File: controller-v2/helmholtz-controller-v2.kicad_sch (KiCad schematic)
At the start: 58 parts, among them J1 Screw_Terminal_01x02, J2 Screw_Terminal_01x02, J3 Screw_Terminal_01x02, J4 Screw_Terminal_01x02, J5 Conn_01x04, U1 BDS63150AFM, U2 BDS63150AFM, U3 INA226, U4 INA226, U5 BDS63150AFM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

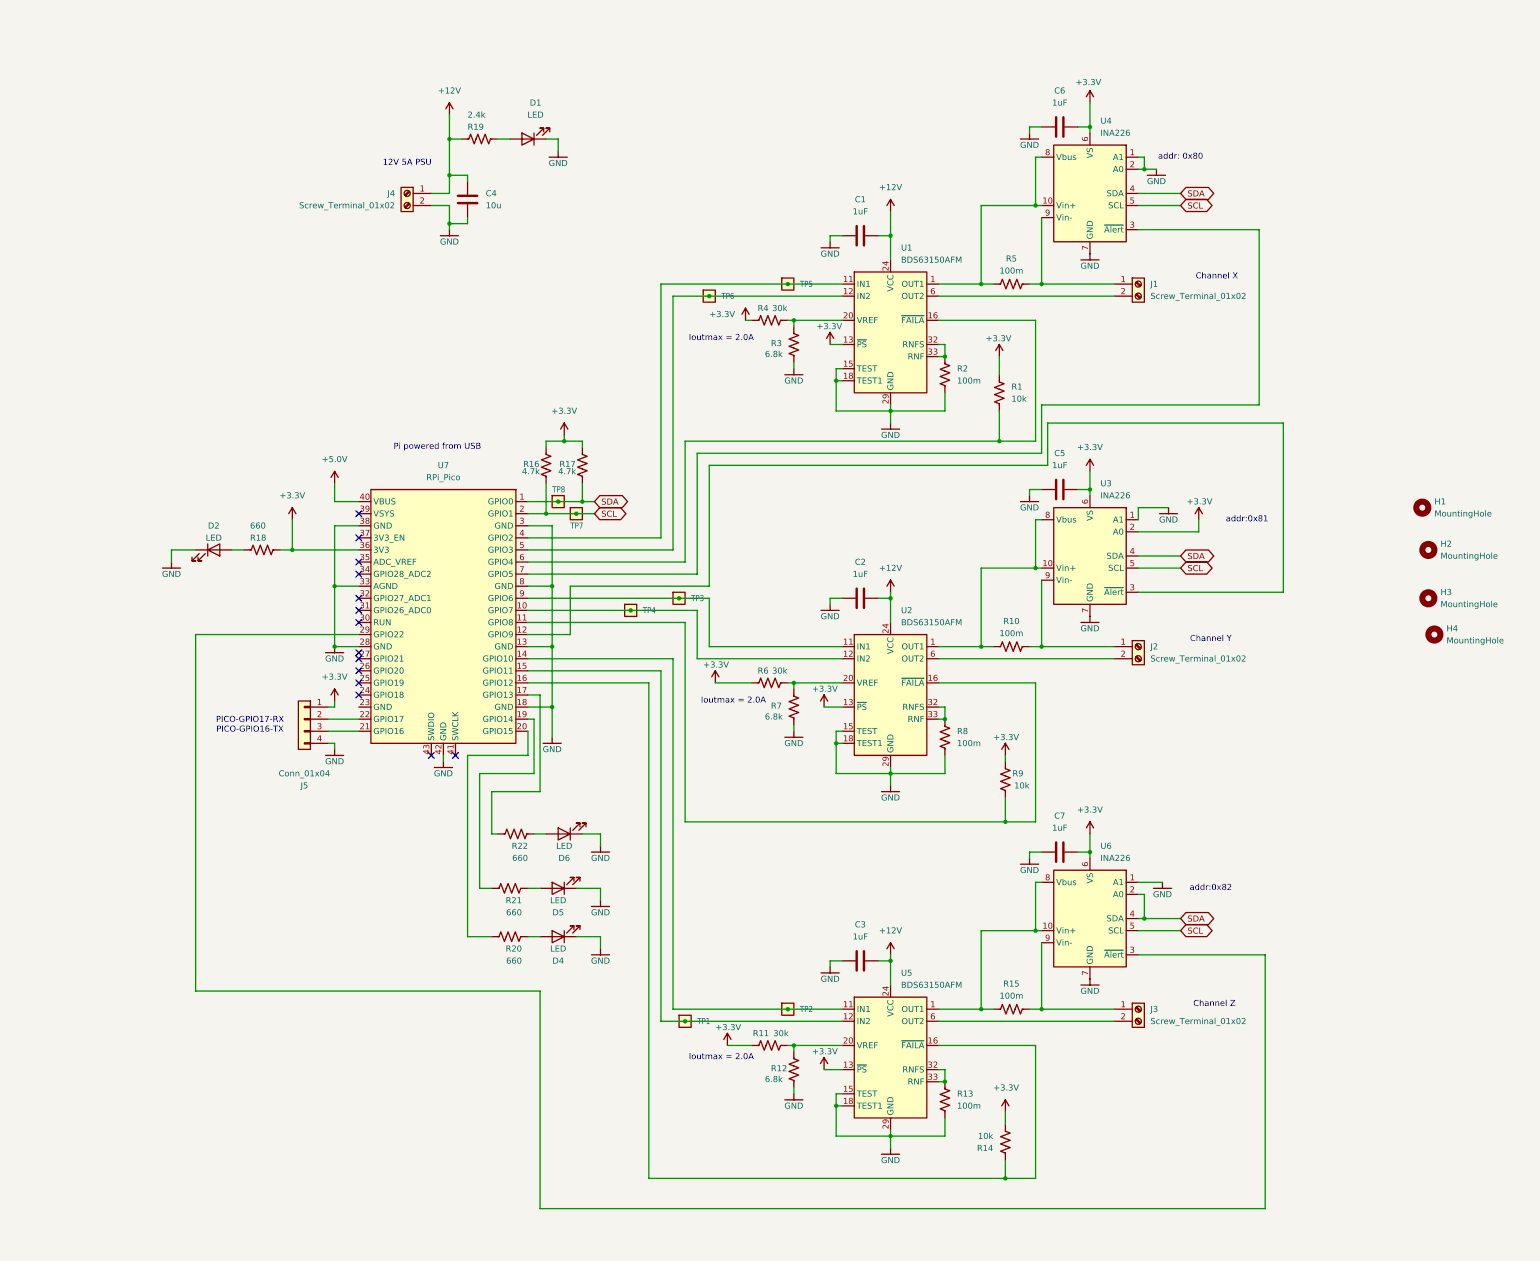
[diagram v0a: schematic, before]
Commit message: fix schematic and layout sync issues. Begin reworking layout to reduce side flipping.
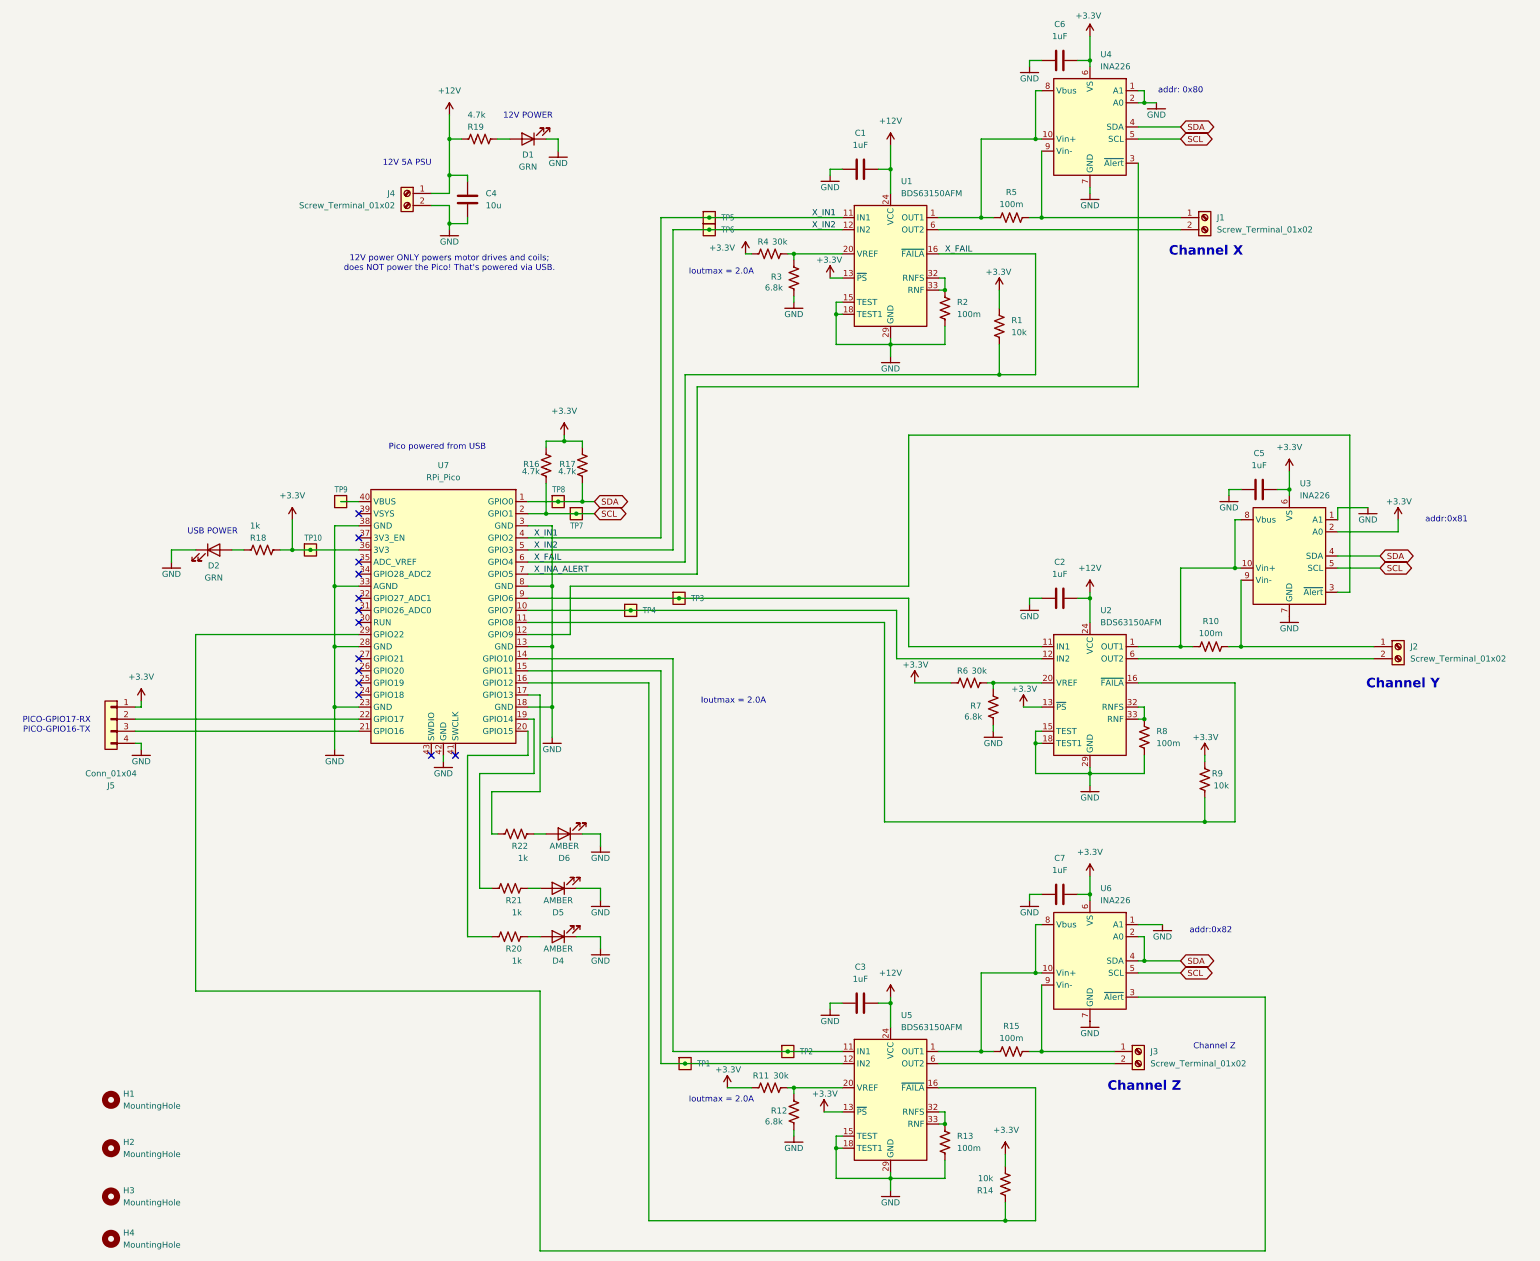
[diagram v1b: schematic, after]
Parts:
- added TP10, TP9: Test-Point, oresat-misc:TestPoint-0.75mm-th, symbol oresat-misc:Test-Point-0.75mm-th
- D1, D2: value LED -> GRN
- D4, D5, D6: value LED -> AMBER
- R18, R20, R21, R22: value 660 -> 1k
- R19: value 2.4k -> 4.7k
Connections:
- net +3.3V: now also TP10.1
- net GND: now also U7.23 (GND)
- net X_IN1: now reaches TP5.1, U1.11 (IN1), U7.4 (GPIO2)
- net X_IN2: now reaches TP6.1, U1.12 (IN2), U7.5 (GPIO3)
- net X_FAIL: now reaches R1.2, U1.16 (~{FAILA}), U7.6 (GPIO4)
- net X_INA_ALERT: now reaches U4.3 (~{Alert}), U7.7 (GPIO5)
- net +5.0V: no longer names the net of U7.40 (VBUS)
- net +5.0V: now also TP9.1
- no-connect marks 14 -> 13
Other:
- note added: "12V POWER"
- note added: "12V power ONLY powers motor drives and coils; does NOT power the Pico! That's powered via USB."
- note added: "Pico powered from USB"
- note added: "USB POWER"
- note removed: "Pi powered from USB"
- company: (none) -> Portland State Aerospace Society
- moved on the sheet: C1, C2, C3, C5, C6, C7, H1, H2, H3, H4, J1, J2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

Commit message: Filled out BOM
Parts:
- C1, C2, C3, C5, C6, C7: DIS (none) -> Digikey; DPN (none) -> 1276-1066-1-ND; MFR (none) -> Samsung Electro-Mechanics; MPN (none) -> CL21B105KAFNNNE
- C4: DIS (none) -> Digikey; DPN (none) -> 1276-2891-1-ND; MFR (none) -> Samsung Electro-Mechanics; MPN (none) -> CL21A106KAYNNNE
- D1, D2: DIS (none) -> Digikey; DPN (none) -> 1830-1062-1-ND; MFR (none) -> Inolux; MPN (none) -> IN-S63AT5G
- D4, D5, D6: DIS (none) -> Digikey; DPN (none) -> 1830-1064-1-ND; MFR (none) -> Inolux; MPN (none) -> IN-S63AT5A
- J1, J2, J3, J4: DIS (none) -> Digikey; DPN (none) -> 277-5719-ND; MFR (none) -> Phoenix Contact; MPN (none) -> 1751248
- J5: DIS (none) -> Digikey; DPN (none) -> WM2702-ND; MFR (none) -> Molex; MPN (none) -> 0022112042
- R1, R14, R9: DIS (none) -> Digikey; DPN (none) -> RMCF0603FT10K0CT-ND; MFR (none) -> Stackpole Electronics Inc; MPN (none) -> RMCF0603FT10K0
- R10, R13, R15, R2, R5, R8: DIS (none) -> Digikey; DPN (none) -> CSR1206FTR100CT-ND; MFR (none) -> Stackpole Electronics Inc; MPN (none) -> CSR1206FTR100
- R11, R4, R6: DIS (none) -> Digikey; DPN (none) -> 541-5344-1-ND; MFR (none) -> Vishay Dale; MPN (none) -> CRCW060330K0FKEAC
- R12, R3, R7: DIS (none) -> Digikey; DPN (none) -> 311-6.8KGRCT-ND; MFR (none) -> YAGEO; MPN (none) -> RC0603JR-076K8L
- R16, R17, R19: DIS (none) -> Digikey; DPN (none) -> 311-4.70KHRCT-ND; MFR (none) -> YAGEO; MPN (none) -> RC0603FR-074K7L
- R18, R20, R21, R22: DIS (none) -> Digikey; DPN (none) -> RMCF0603FT1K00CT-ND; MFR (none) -> Stackpole Electronics Inc; MPN (none) -> RMCF0603FT1K00
- U1, U2, U5: DIS (none) -> Digikey; DPN (none) -> BD63150AFM-E2CT-ND; MFR (none) -> Rohm Semiconductor; MPN (none) -> BD63150AFM-E2
- U3, U4, U6: DIS (none) -> Digikey; DPN (none) -> 296-29100-1-ND; MFR (none) -> Texas Instruments; MPN (none) -> INA226AIDGST
- U7: DIS (none) -> Digikey; DPN (none) -> 2648-SC0915CT-ND; MFR (none) -> Raspberry Pi; MPN (none) -> SC0915
